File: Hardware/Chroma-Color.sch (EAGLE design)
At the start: 41 parts, among them J1 15-91-1102, U1 EP4CE6E22C8N, U2 ADP3338AKCZ-3.3-RL, U3 ADP3338AKCZ-2.5-RL, U4 NCV565ST12T3G, U5 M25P40-VMN6TPBCT

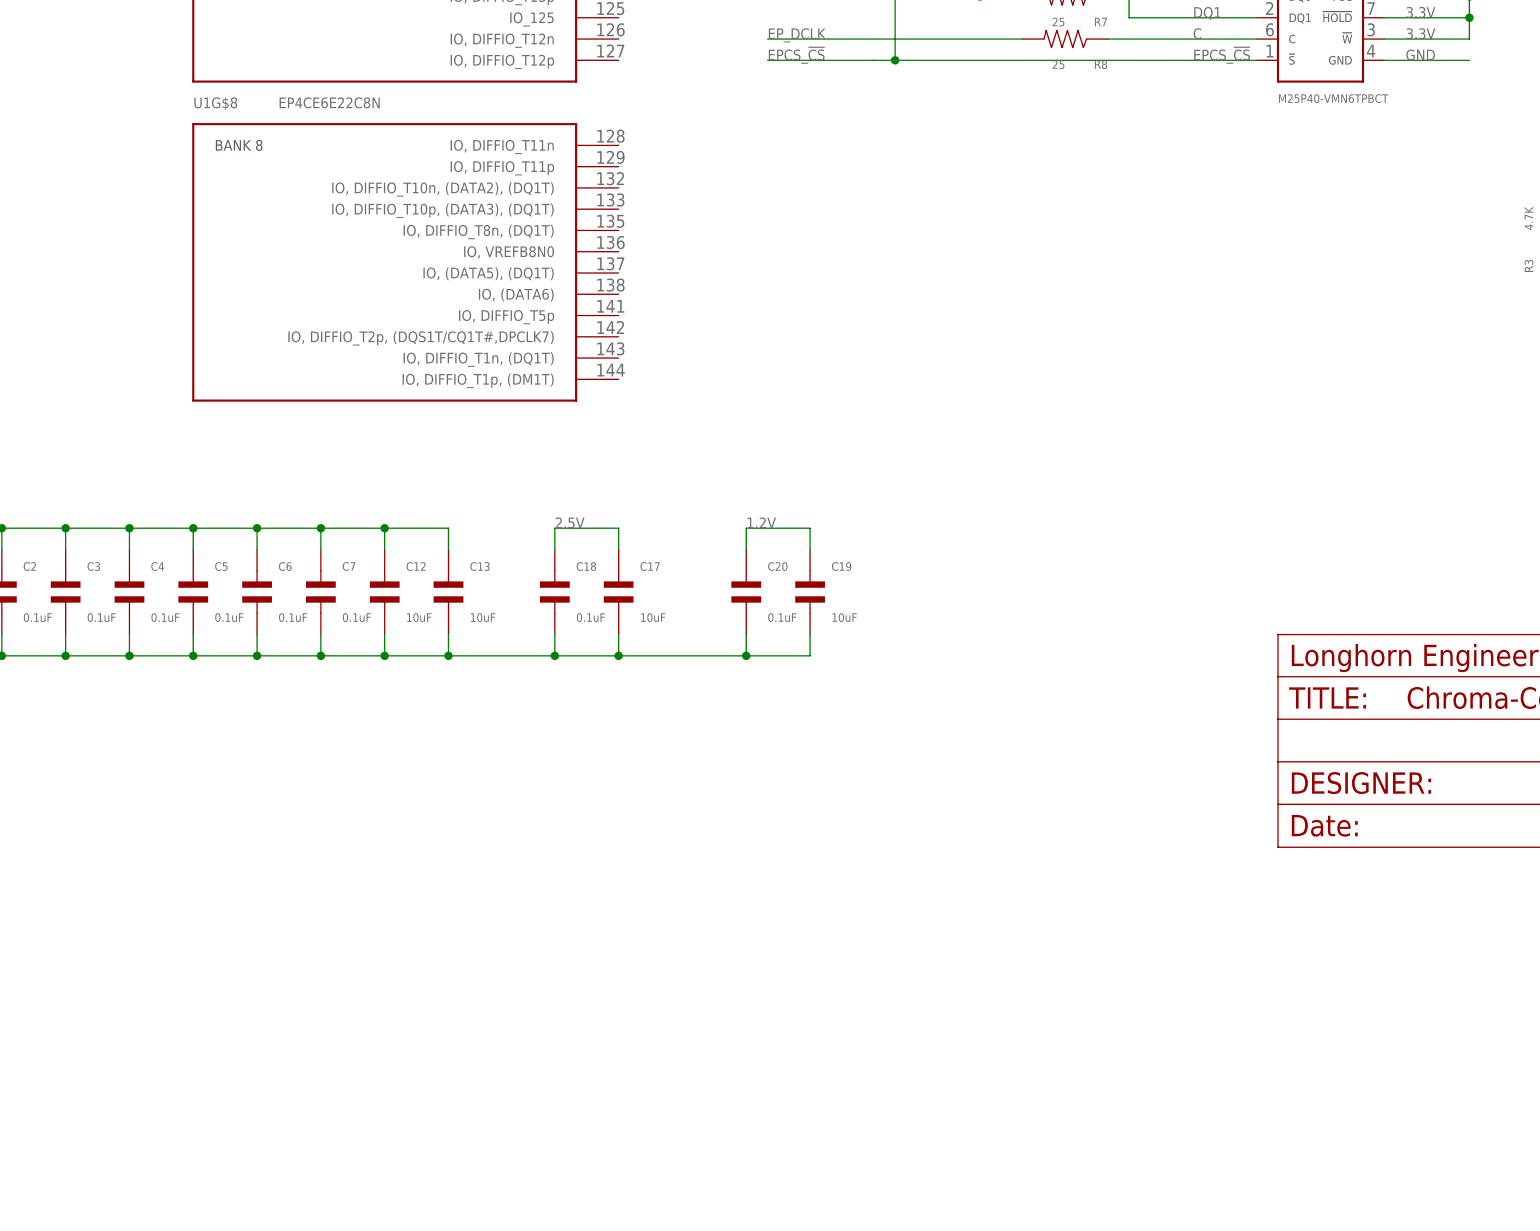
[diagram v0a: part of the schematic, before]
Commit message: Added connectors and crystal
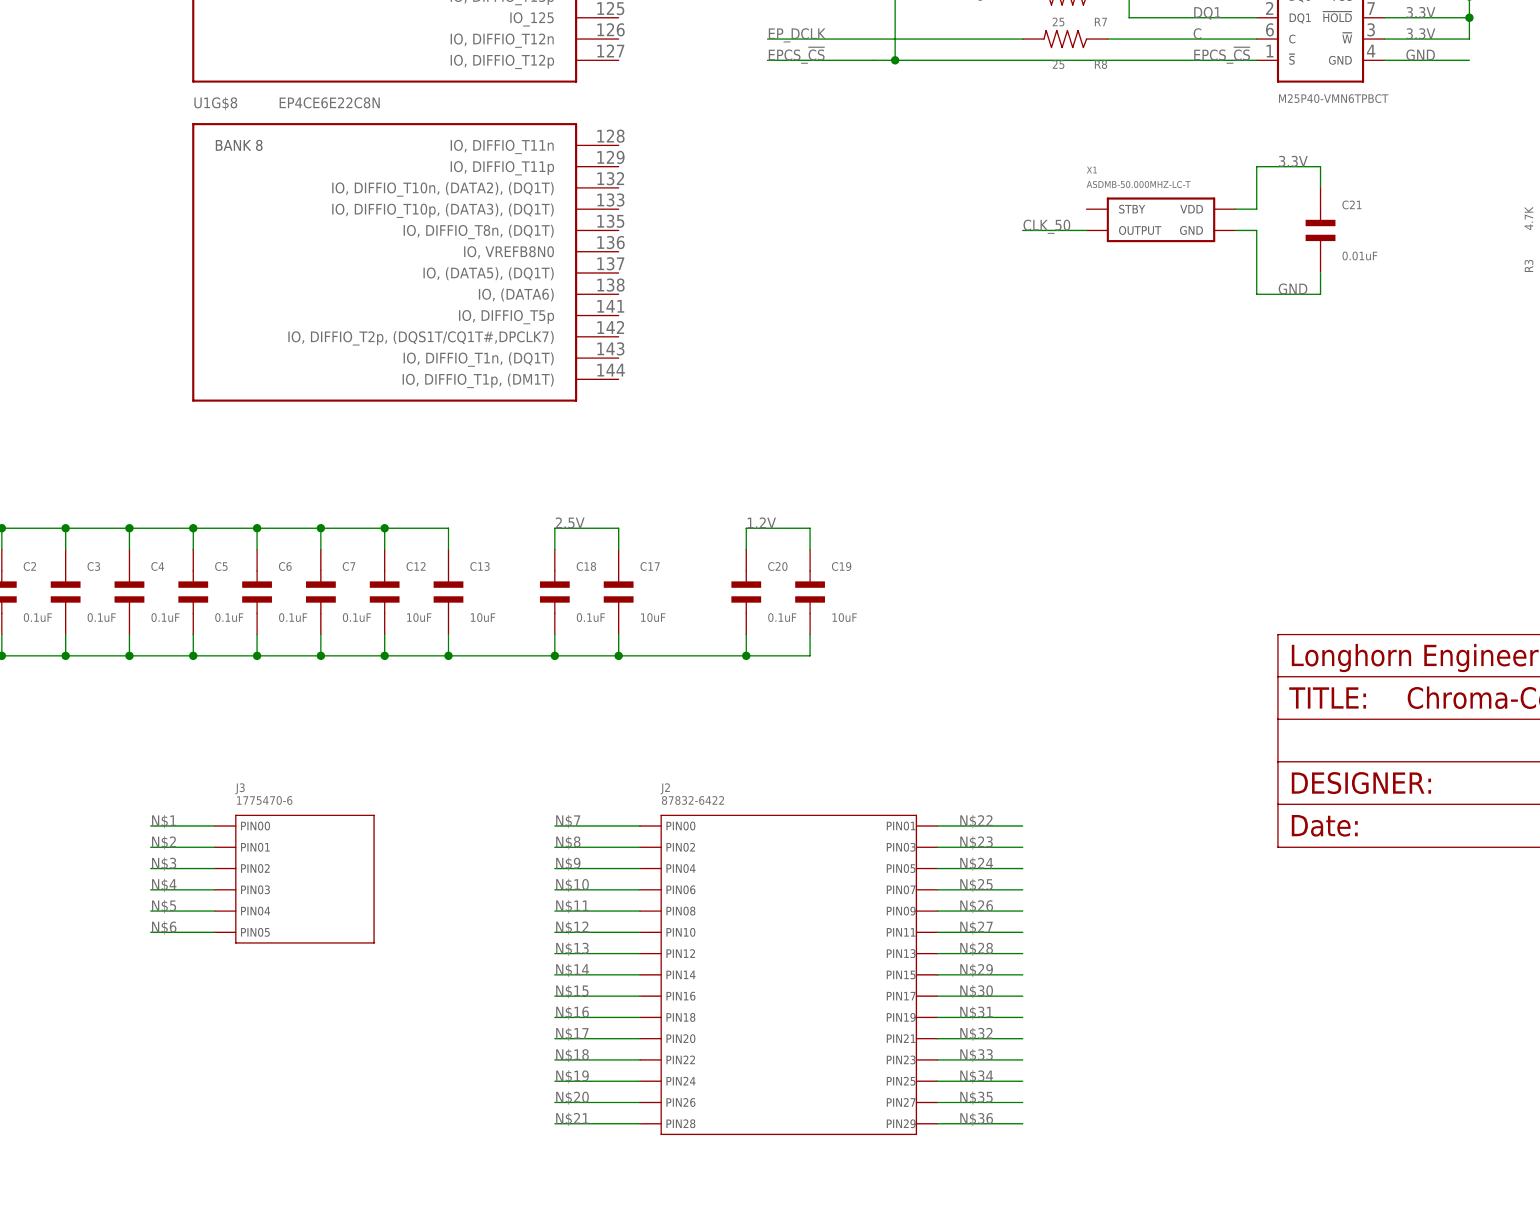
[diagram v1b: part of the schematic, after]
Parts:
- added C21: 0.01uF, MF_Passives:CAPACITOR_NP_0603
- added J2: 87832-6422, PP_Connectors:87832-6422
- added J3: 1775470-6, PP_Connectors:1775470-6
- added X1: ASDMB-50.000MHZ-LC-T, PP_FreqCtrl:ASDMB
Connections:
- new net N$1: J3.PIN0
- new net N$10: J2.PIN6
- new net N$11: J2.PIN8
- new net N$12: J2.PIN11
- new net N$13: J2.PIN12
- new net N$14: J2.PIN14
- new net N$15: J2.PIN16
- new net N$16: J2.PIN18
- new net N$17: J2.PIN21
- new net N$18: J2.PIN22
- new net N$19: J2.PIN24
- new net N$2: J3.PIN1
- new net N$20: J2.PIN26
- new net N$21: J2.PIN28
- new net N$22: J2.PIN1
- new net N$23: J2.PIN3
- new net N$24: J2.PIN5
- new net N$25: J2.PIN7
- new net N$26: J2.PIN9
- new net N$27: J2.PIN10
- new net N$28: J2.PIN13
- new net N$29: J2.PIN15
- new net N$3: J3.PIN2
- new net N$30: J2.PIN17
- new net N$31: J2.PIN19
- new net N$32: J2.PIN20
- new net N$33: J2.PIN23
- new net N$34: J2.PIN25
- new net N$35: J2.PIN27
- new net N$36: J2.PIN29
- new net N$4: J3.PIN3
- new net N$5: J3.PIN4
- new net N$6: J3.PIN5
- new net N$7: J2.PIN0
- new net N$8: J2.PIN2
- new net N$9: J2.PIN4
- net 3.3V: now also C21.P$1, X1.VDD
- net CLK_50: now also X1.OUTPUT
- net GND: now also C21.P$2, X1.GND

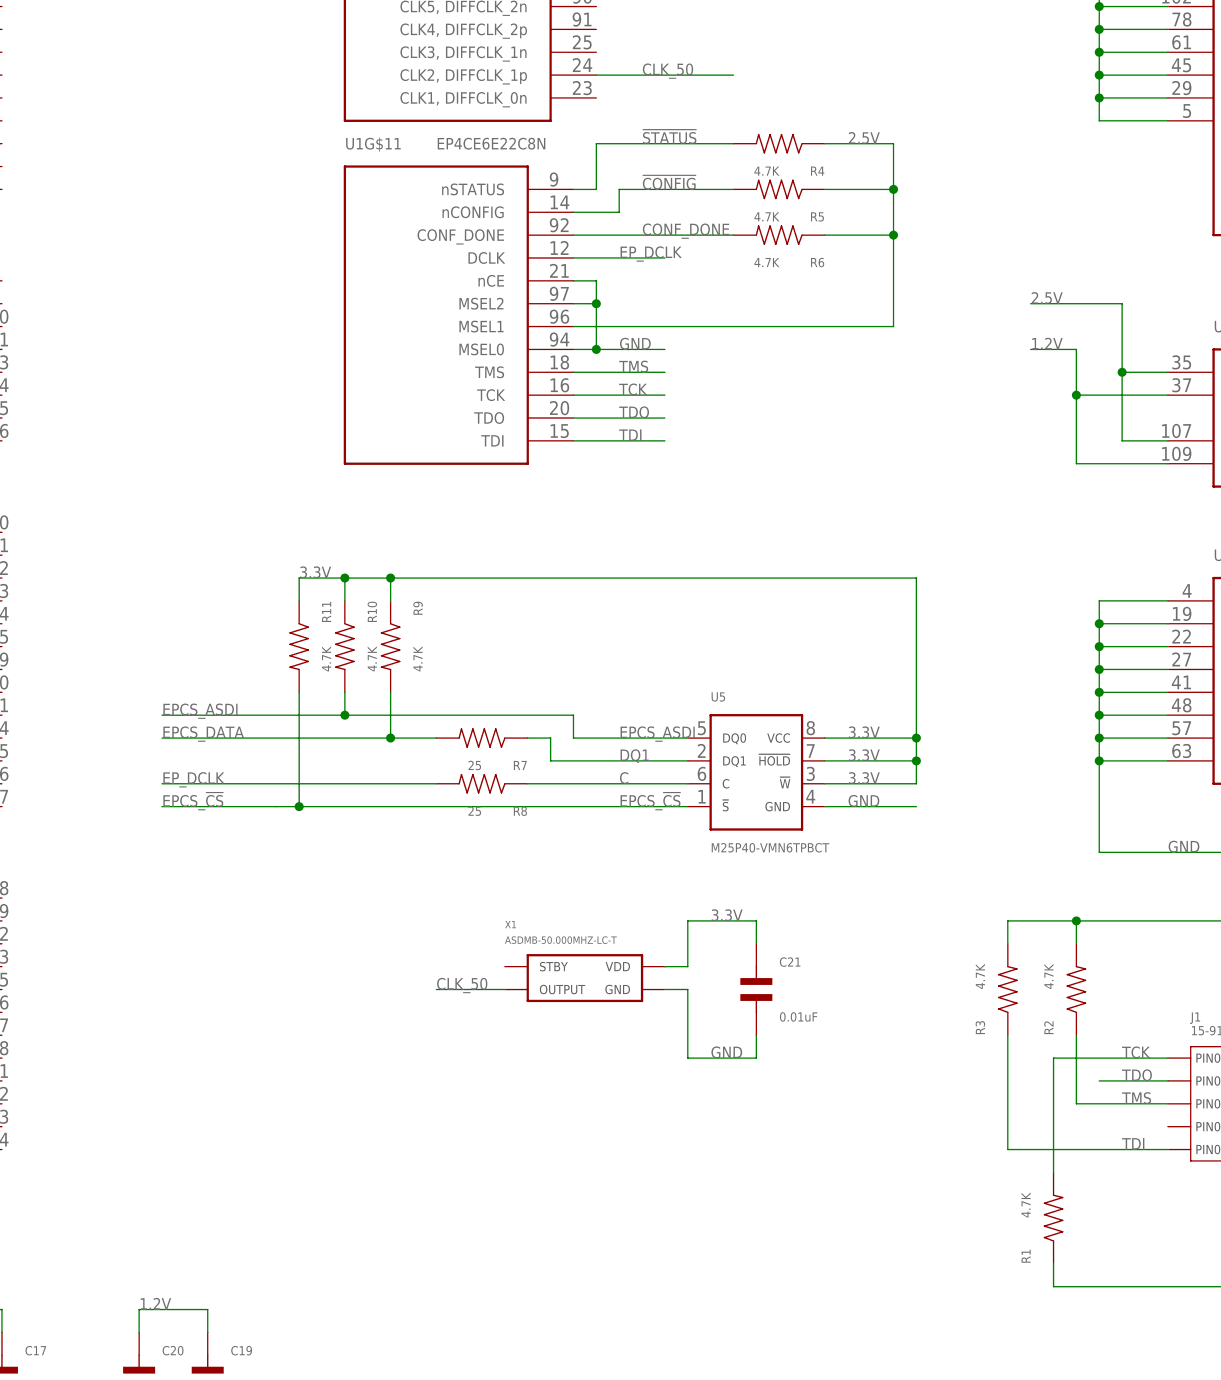
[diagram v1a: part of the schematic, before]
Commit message: Changed 4.7K to 10K resistors.
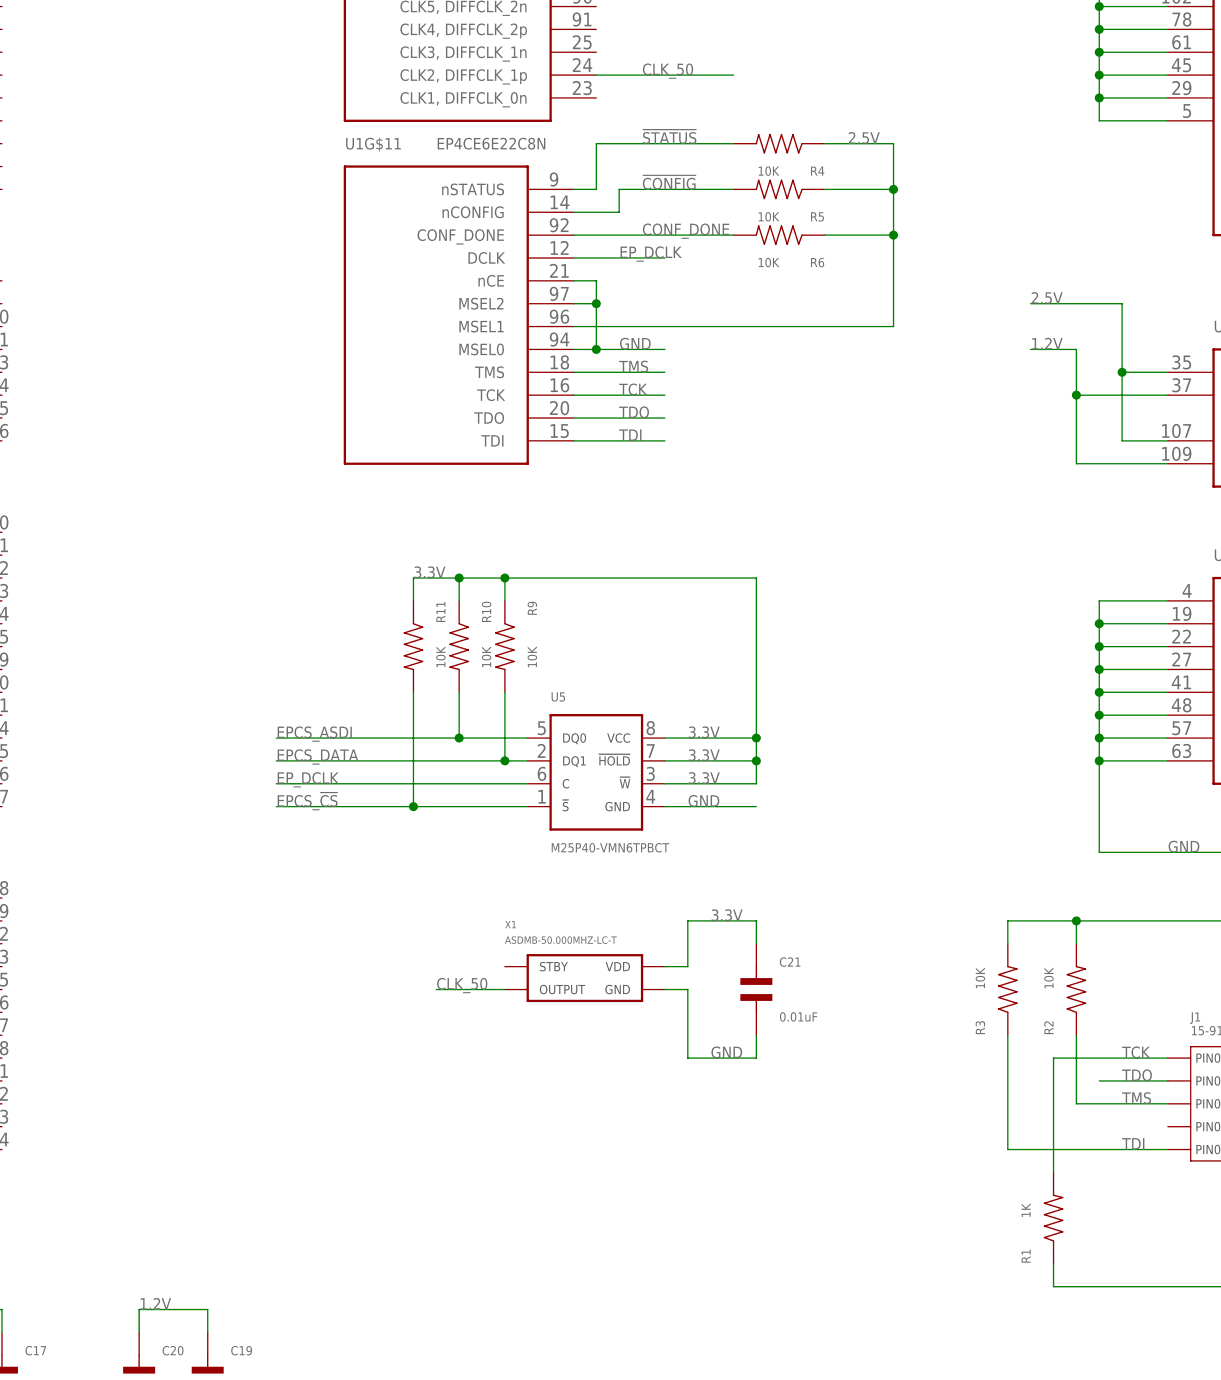
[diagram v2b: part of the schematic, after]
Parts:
- removed R7, R8: 25, MF_Passives:RESISTOR_0805
- R1: value 4.7K -> 1K
- R10, R11, R2, R3, R4, R5, R6, R9: value 4.7K -> 10K
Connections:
- removed net C: R8.P$1, U5.C
- removed net DQ1: R7.P$1, U5.DQ1
- net EPCS_DATA: now also U5.DQ1; no longer R7.P$2
- net EP_DCLK: now also U5.C; no longer R8.P$2
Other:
- moved on the sheet: R10, R11, R9, U5
